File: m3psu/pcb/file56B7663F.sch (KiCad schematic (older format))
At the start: 0 parts

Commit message: Started working on the Dc/DC converter.
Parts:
- added C? (x11): C, symbol C
- added IC?: LTC3887, agg:QFN-40-EP-LTC-UJ, symbol LTC3887
- added L? (x2): L, symbol L
- added Q? (x4): NFET, symbol NFET
- added R? (x6): R, symbol R
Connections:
- new net: C?.1, IC?.1 (V_SENSE_0+), R?.1, R?.1
- new net: C?.1, IC?.22 (VDD_25)
- new net: C?.1, IC?.25 (VDD_33)
- new net: C?.1, IC?.27 (V_SENSE_1), R?.2, R?.2
- new net: C?.2, IC?.29 (SW1), L?.1, Q?.2 (S), Q?.3 (D)
- new net: C?.1, IC?.3 (I_SENSE_1+), R?.1
- new net: IC?.30 (TG1), Q?.1 (G)
- new net: C?.1, IC?.31 (BOOST1)
- new net: IC?.32 (BG1), Q?.1 (G)
- new net: C?.1, C?.1, IC?.33 (INTVCC)
- new net: IC?.36 (BG0), Q?.1 (G)
- new net: C?.2, IC?.37 (BOOST0)
- new net: IC?.38 (TG0), Q?.1 (G)
- new net: C?.1, IC?.39 (SW0), L?.2, Q?.2 (S), Q?.3 (D)
- new net: C?.2, IC?.4 (I_SENSE_1-), R?.1
- new net: C?.1, IC?.6 (I_SENSE_0+), R?.2
- new net: C?.2, IC?.7 (I_SENSE_0-), R?.2
- new net: L?.2, R?.1, R?.2
- new net: L?.1, R?.1, R?.2
- new net GND: C?.2, C?.2, C?.2, C?.2, C?.2, C?.2, C?.2, IC?.2 (V_SENSE_0-), IC?.34 (GND), IC?.EP (GND), Q?.2 (S), Q?.2 (S)
- new net VCC: C?.1, IC?.35 (V_IN), Q?.3 (D), Q?.3 (D)

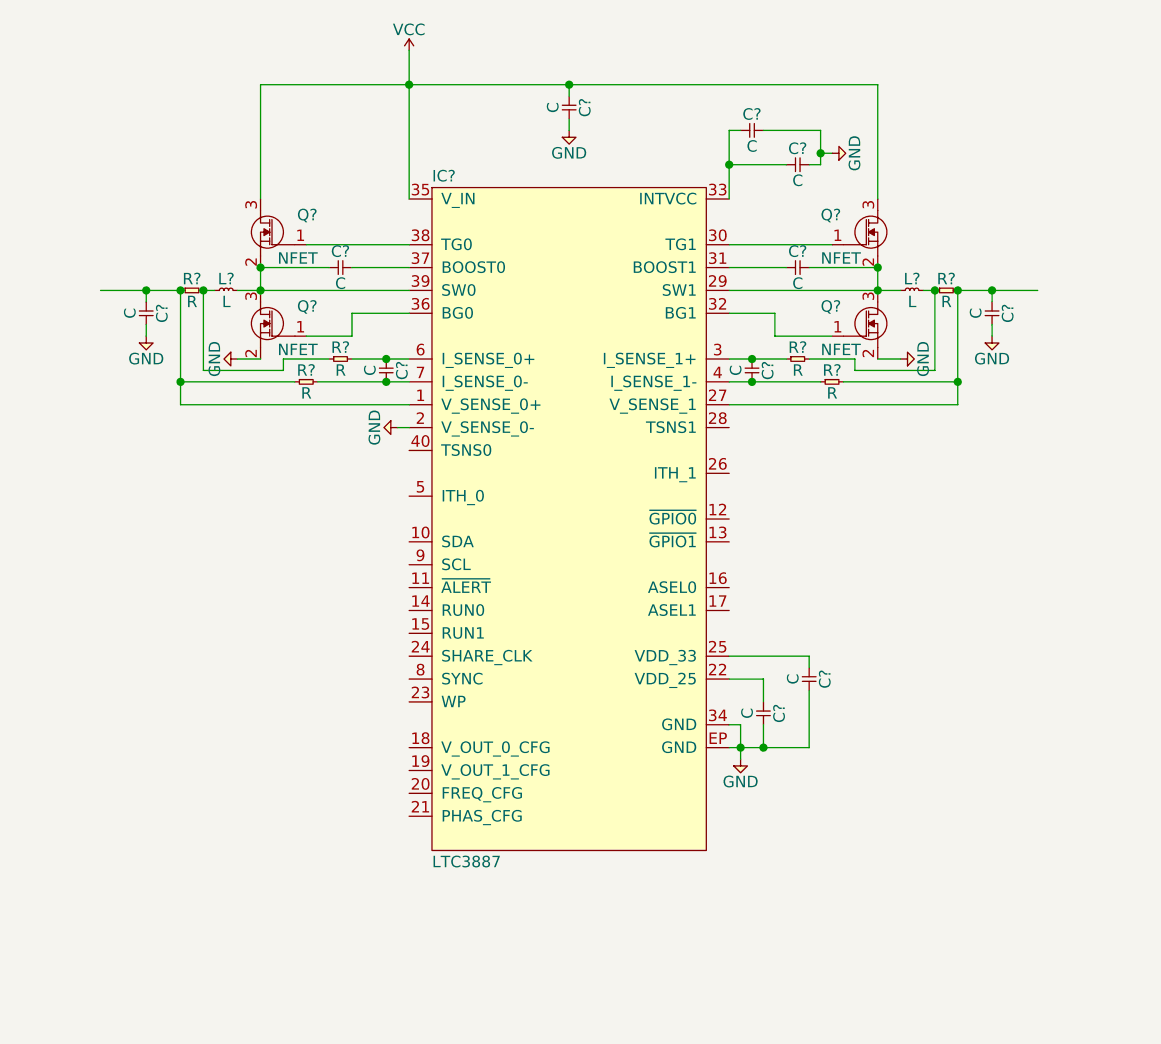
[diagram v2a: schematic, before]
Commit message: Wired up the DC/DC converter (not all values done yet). Updated agg-kicad.
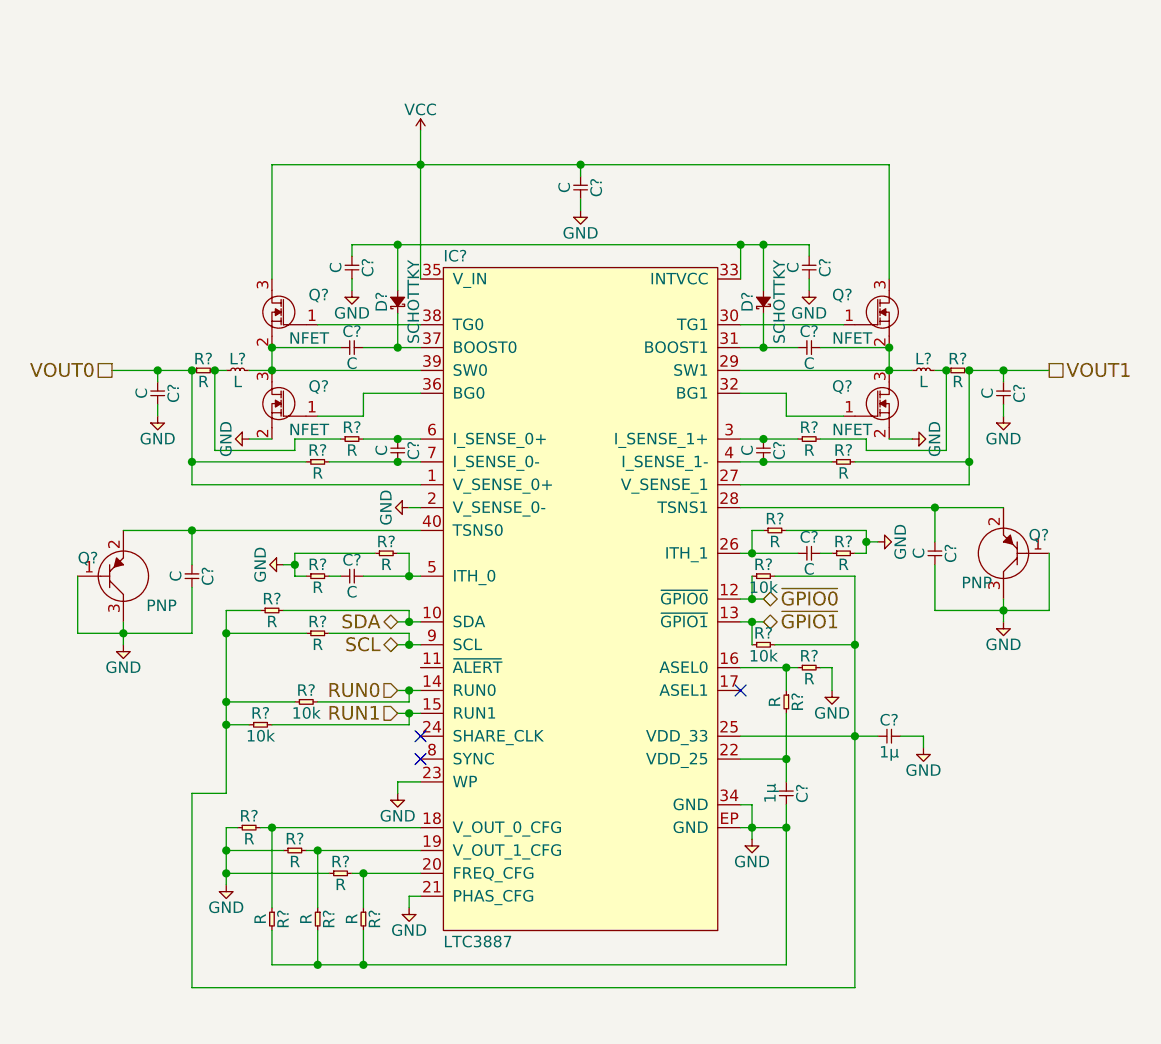
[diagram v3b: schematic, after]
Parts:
- removed C?: C, symbol C
- added C? (x5): C, symbol C
- added D? (x2): SCHOTTKY, symbol SCHOTTKY
- added Q? (x2): PNP, symbol PNP
- added R? (x4): 10k, symbol R
- added R? (x14): R, symbol R
- C? (x2): value C -> 1µ
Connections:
- net GND: now also IC?.21 (PHAS_CFG), IC?.23 (WP), C?.2, C?.2, C?.2, Q?.1 (B), Q?.1 (B), Q?.3 (C), Q?.3 (C), R?.1, R?.1, R?.1, R?.1, R?.1, R?.2, R?.2, R?.2, R?.2, R?.2, R?.2
- net VOUT0: now reaches C?.1, IC?.1 (V_SENSE_0+), R?.1, R?.1
- net SDA: now reaches IC?.10 (SDA)
- net SDA: now also R?.2
- net ~GPIO0: now reaches IC?.12 (~GPIO0)
- net ~GPIO0: now also R?.1
- net ~GPIO1: now reaches IC?.13 (~GPIO1)
- net ~GPIO1: now also R?.1
- net RUN0: now reaches IC?.14 (RUN0)
- net RUN0: now also R?.2
- net RUN1: now reaches IC?.15 (RUN1)
- net RUN1: now also R?.2
- net at IC?.16 (ASEL0): now also R?.1, R?.1
- net at IC?.18 (V_OUT_0_CFG): now also R?.1, R?.2
- net at IC?.19 (V_OUT_1_CFG): now also R?.1, R?.2
- net at IC?.20 (FREQ_CFG): now also R?.1, R?.2
- net at C?.1, IC?.22 (VDD_25): now also R?.2
- net at C?.1, IC?.25 (VDD_33): now also R?.1, R?.1, R?.1, R?.1, R?.2, R?.2
- net at IC?.26 (ITH_1): now also C?.1, R?.1
- net VOUT1: now reaches C?.1, IC?.27 (V_SENSE_1), R?.2, R?.2
- net at IC?.28 (TSNS1): now also C?.1, Q?.2 (E)
- net at C?.1, IC?.31 (BOOST1): now also D?.1
- net at C?.1, IC?.33 (INTVCC): now also C?.1, D?.2, D?.2
- net at C?.2, IC?.37 (BOOST0): now also D?.1
- net at IC?.40 (TSNS0): now also C?.1, Q?.2 (E)
- net at IC?.5 (ITH_0): now also C?.2, R?.2
- net SCL: now reaches IC?.9 (SCL)
- net SCL: now also R?.2
- new net: C?.2, R?.1
- new net: C?.1, R?.2
- no-connect marks 0 -> 3
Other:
- moved on the sheet: C?, IC?, L?, Q?, R?

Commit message: Updated some of the parts of the schematics.
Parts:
- removed C? (x2): C, symbol C
- removed Q? (x2): PNP, symbol PNP
- removed R? (x2): 10k, symbol R
- removed R? (x2): R, symbol R
- added C? (x2): 220p, symbol C
- C? (x2): value C -> 1n
- C? (x2): value C -> 4n7
- R? (x2): value R -> 10m
- R? (x4): value R -> 100
- R? (x2): value R -> 4k7
- R? (x2): value R -> 4.99k
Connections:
- net GND: now also IC?.28 (TSNS1), IC?.40 (TSNS0), C?.1, C?.2
- net at C?.1, IC?.26 (ITH_1): now also C?.1
- net at C?.2, IC?.5 (ITH_0): now also C?.2
- net ~GPIO0: no longer names the net of IC?.12 (~GPIO0)
- net ~GPIO1: no longer names the net of IC?.13 (~GPIO1)
- no-connect marks 3 -> 5

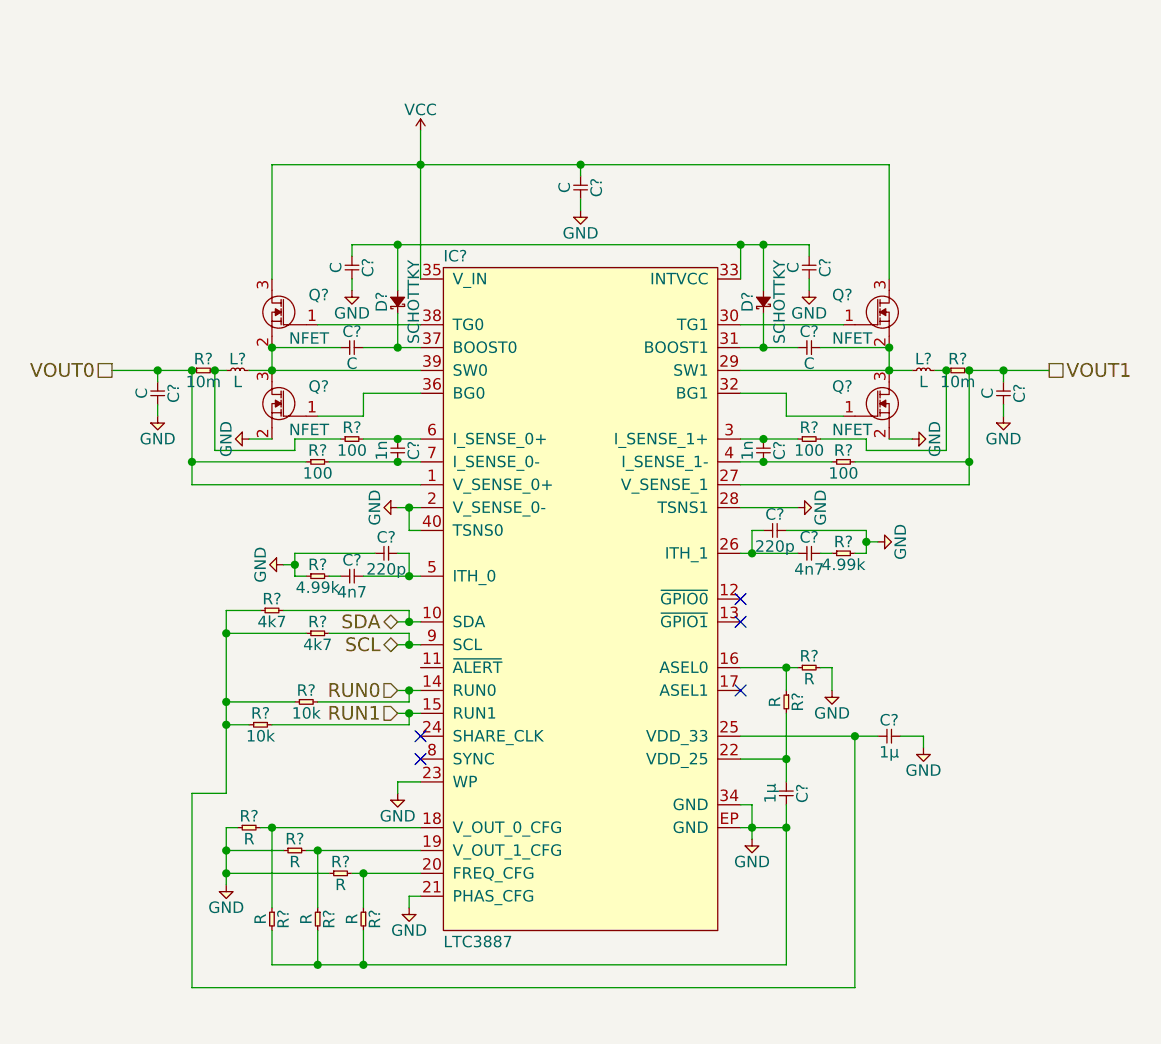
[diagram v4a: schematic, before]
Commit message: Caclulated values to some components. Updated notes.txt.
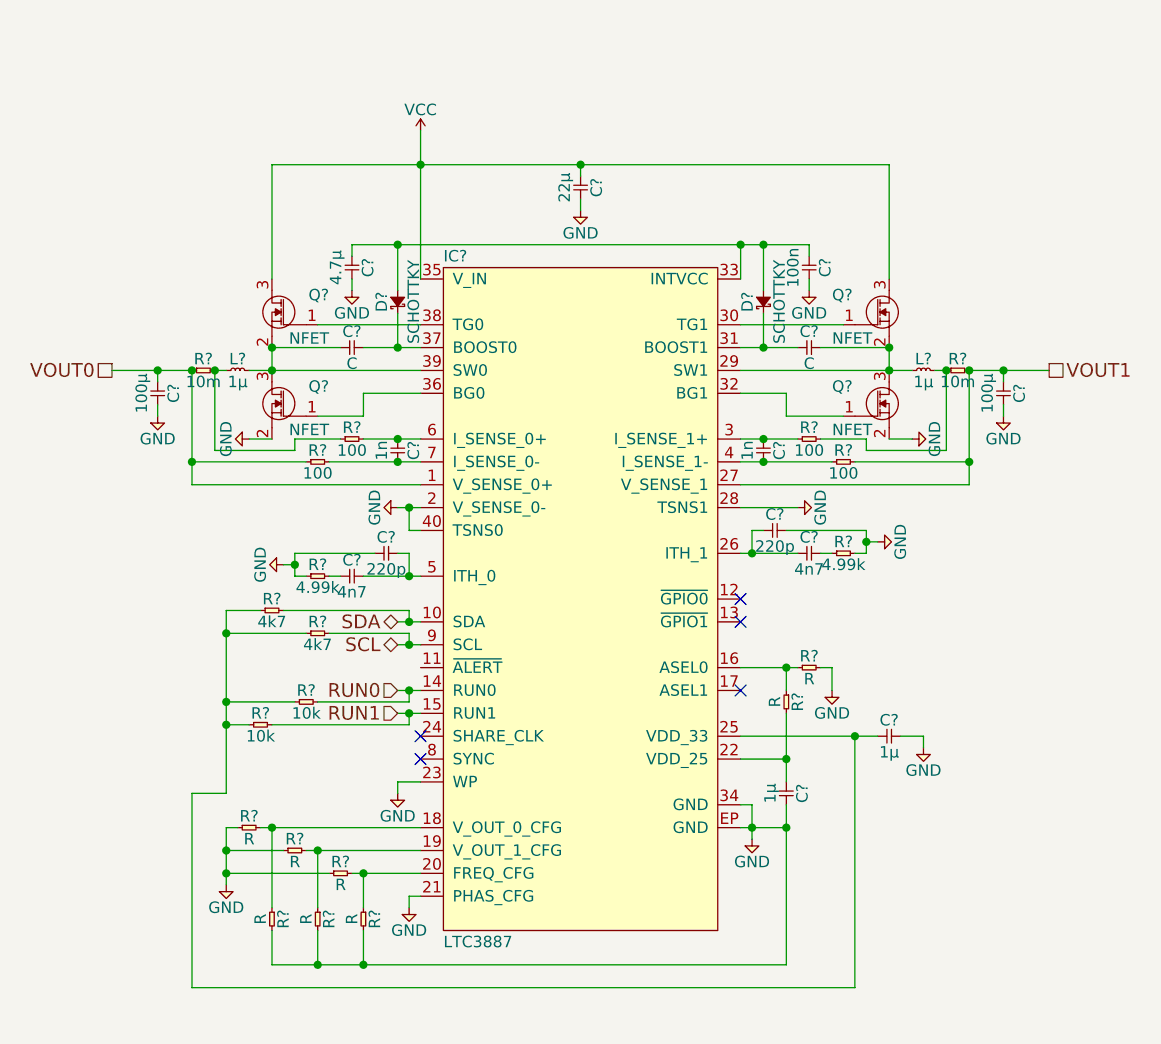
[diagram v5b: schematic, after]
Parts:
- C?: value C -> 4.7µ
- C?: value C -> 22µ
- C? (x2): value C -> 100µ
- C?: value C -> 100n
- L? (x2): value L -> 1µ
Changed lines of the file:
@@
 P 7050 2850
 F 0 "L?" H 7100 2900 50  0000 C CNN
-F 1 "L" H 7100 2800 50  0000 C CNN
+F 1 "1µ" H 7100 2800 50  0000 C CNN
 F 2 "" H 7050 2850 50  0001 C CNN
 F 3 "" H 7050 2850 50  0001 C CNN
@@
 P 4050 2850
 F 0 "L?" H 4100 2900 50  0000 C CNN
-F 1 "L" H 4100 2800 50  0000 C CNN
+F 1 "1µ" H 4100 2800 50  0000 C CNN
 F 2 "" H 4050 2850 50  0001 C CNN
 F 3 "" H 4050 2850 50  0001 C CNN
@@
 P 4600 2350
 F 0 "C?" H 4650 2420 50  0000 C CNN
-F 1 "C" H 4650 2280 50  0000 C CNN
+F 1 "4.7µ" H 4650 2280 50  0000 C CNN
 F 2 "" H 4600 2350 50  0001 C CNN
 F 3 "" H 4600 2350 50  0001 C CNN
@@
 P 5600 2000
 F 0 "C?" H 5650 2070 50  0000 C CNN
-F 1 "C" H 5650 1930 50  0000 C CNN
+F 1 "22µ" H 5650 1930 50  0000 C CNN
 F 2 "" H 5600 2000 50  0001 C CNN
 F 3 "" H 5600 2000 50  0001 C CNN
@@
 P 7450 2900
 F 0 "C?" H 7500 2970 50  0000 C CNN
-F 1 "C" H 7500 2830 50  0000 C CNN
+F 1 "100µ" H 7500 2830 50  0000 C CNN
 F 2 "" H 7450 2900 50  0001 C CNN
 F 3 "" H 7450 2900 50  0001 C CNN
@@
 P 3750 2900
 F 0 "C?" H 3800 2970 50  0000 C CNN
-F 1 "C" H 3800 2830 50  0000 C CNN
+F 1 "100µ" H 3800 2830 50  0000 C CNN
 F 2 "" H 3750 2900 50  0001 C CNN
 F 3 "" H 3750 2900 50  0001 C CNN
@@
 P 6600 2350
 F 0 "C?" H 6650 2420 50  0000 C CNN
-F 1 "C" H 6650 2280 50  0000 C CNN
+F 1 "100n" H 6650 2280 50  0000 C CNN
 F 2 "" H 6600 2350 50  0001 C CNN
 F 3 "" H 6600 2350 50  0001 C CNN

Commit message: Finished the component values and parts for the DC/DC Converter.
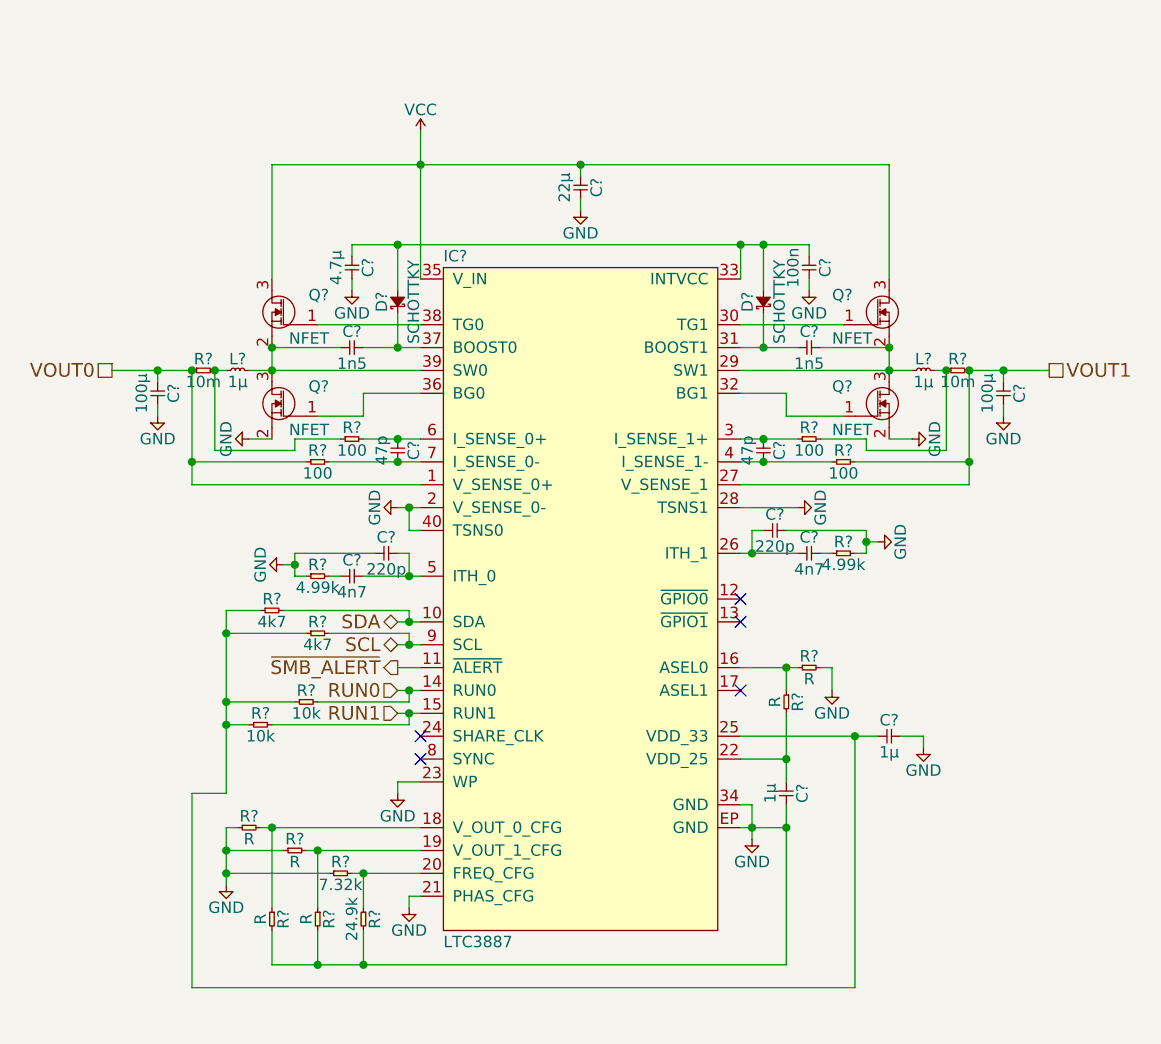
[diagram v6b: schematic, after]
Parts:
- C? (x2): value C -> 1n5
- C? (x2): value 1n -> 47p
- R?: value R -> 24.9k
- R?: value R -> 7.32k
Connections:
- net ~SMB_ALERT: now reaches IC?.11 (~ALERT)
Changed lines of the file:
@@
 P 6550 2750
 F 0 "C?" H 6600 2820 50  0000 C CNN
-F 1 "C" H 6600 2680 50  0000 C CNN
+F 1 "1n5" H 6600 2680 50  0000 C CNN
 F 2 "" H 6550 2750 50  0001 C CNN
 F 3 "" H 6550 2750 50  0001 C CNN
@@
 P 4550 2750
 F 0 "C?" H 4600 2820 50  0000 C CNN
-F 1 "C" H 4600 2680 50  0000 C CNN
+F 1 "1n5" H 4600 2680 50  0000 C CNN
 F 2 "" H 4550 2750 50  0001 C CNN
 F 3 "" H 4550 2750 50  0001 C CNN
@@
 P 6400 3150
 F 0 "C?" H 6450 3220 50  0000 C CNN
-F 1 "1n" H 6450 3080 50  0000 C CNN
+F 1 "47p" H 6450 3080 50  0000 C CNN
 F 2 "" H 6400 3150 50  0001 C CNN
 F 3 "" H 6400 3150 50  0001 C CNN
@@
 P 4800 3150
 F 0 "C?" H 4850 3220 50  0000 C CNN
-F 1 "1n" H 4850 3080 50  0000 C CNN
+F 1 "47p" H 4850 3080 50  0000 C CNN
 F 2 "" H 4800 3150 50  0001 C CNN
 F 3 "" H 4800 3150 50  0001 C CNN
@@
 P 4650 5200
 F 0 "R?" H 4700 5250 50  0000 C CNN
-F 1 "R" H 4700 5150 50  0000 C CNN
+F 1 "24.9k" H 4700 5150 50  0000 C CNN
 F 2 "" H 4650 5200 50  0001 C CNN
 F 3 "" H 4650 5200 50  0001 C CNN
@@
 P 4500 5050
 F 0 "R?" H 4550 5100 50  0000 C CNN
-F 1 "R" H 4550 5000 50  0000 C CNN
+F 1 "7.32k" H 4550 5000 50  0000 C CNN
 F 2 "" H 4500 5050 50  0001 C CNN
 F 3 "" H 4500 5050 50  0001 C CNN
@@
 	1    0    0    -1
 $EndComp
+Wire Wire Line
+	4900 4150 4800 4150
+Text HLabel 4800 4150 0    60   Output ~ 0
+~SMB_ALERT
 $EndSCHEMATC

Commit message: Add Farnell numbers, for real this time
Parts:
- C? (x2): Farnell (none) -> 1735535
- D? (x2): Farnell (none) -> 2317558
- Q? (x4): Farnell (none) -> 2422226
- R? (x2): value 10m -> 50m; Farnell (none) -> 1506129
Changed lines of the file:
@@
 F 2 "" H 6950 2550 50  0001 C CNN
 F 3 "" H 6950 2550 50  0001 C CNN
+F 4 "2422226" H 6950 2550 60  0001 C CNN "Farnell"
 	1    6950 2550
 	1    0    0    -1
@@
 F 2 "" H 6950 2950 50  0001 C CNN
 F 3 "" H 6950 2950 50  0001 C CNN
+F 4 "2422226" H 6950 2950 60  0001 C CNN "Farnell"
 	1    6950 2950
 	1    0    0    -1
@@
 F 2 "" H 4250 2950 50  0001 C CNN
 F 3 "" H 4250 2950 50  0001 C CNN
+F 4 "2422226" H 4250 2950 60  0001 C CNN "Farnell"
 	1    4250 2950
 	-1   0    0    -1
@@
 F 2 "" H 4250 2550 50  0001 C CNN
 F 3 "" H 4250 2550 50  0001 C CNN
+F 4 "2422226" H 4250 2550 60  0001 C CNN "Farnell"
 	1    4250 2550
 	-1   0    0    -1
@@
 P 7200 2850
 F 0 "R?" H 7250 2900 50  0000 C CNN
-F 1 "10m" H 7250 2800 50  0000 C CNN
+F 1 "50m" H 7250 2800 50  0000 C CNN
 F 2 "" H 7200 2850 50  0001 C CNN
 F 3 "" H 7200 2850 50  0001 C CNN
+F 4 "1506129" H 7200 2850 60  0001 C CNN "Farnell"
 	1    7200 2850
 	1    0    0    -1
@@
 P 3900 2850
 F 0 "R?" H 3950 2900 50  0000 C CNN
-F 1 "10m" H 3950 2800 50  0000 C CNN
+F 1 "50m" H 3950 2800 50  0000 C CNN
 F 2 "" H 3900 2850 50  0001 C CNN
 F 3 "" H 3900 2850 50  0001 C CNN
+F 4 "1506129" H 3900 2850 60  0001 C CNN "Farnell"
 	1    3900 2850
 	1    0    0    -1
@@
 F 2 "" H 7450 2900 50  0001 C CNN
 F 3 "" H 7450 2900 50  0001 C CNN
+F 4 "1735535" H 7450 2900 60  0001 C CNN "Farnell"
 	1    7450 2900
 	0    1    1    0
@@
 F 2 "" H 3750 2900 50  0001 C CNN
 F 3 "" H 3750 2900 50  0001 C CNN
+F 4 "1735535" H 3750 2900 60  0001 C CNN "Farnell"
 	1    3750 2900
 	0    1    1    0
@@
 F 2 "" H 4750 2570 50  0001 C CNN
 F 3 "" H 4850 2670 50  0001 C CNN
+F 4 "2317558" H 4800 2600 60  0001 C CNN "Farnell"
 	1    4800 2600
 	0    -1   -1   0
@@
 F 2 "" H 6350 2570 50  0001 C CNN
 F 3 "" H 6450 2670 50  0001 C CNN
+F 4 "2317558" H 6400 2600 60  0001 C CNN "Farnell"
 	1    6400 2600
 	0    -1   -1   0

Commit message: Add second regulator, inductor Farnell number
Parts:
- removed R? (x2): R, symbol R
- removed R? (x2): 10k, symbol R
- added R? (x2): 100K, symbol R
- L? (x2): Farnell (none) -> 2292535
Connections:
- net GND: now also IC?.16 (ASEL0), R?.2, R?.2
- net RUN0: now also R?.1
- net RUN1: now also R?.1
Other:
- note added: "Address 0x40"
